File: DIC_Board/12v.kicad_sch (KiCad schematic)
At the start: 31 parts, among them Q100 CSD18542KTTT, Q101 CSD18542KTTT, U10 TPS552882RPMR

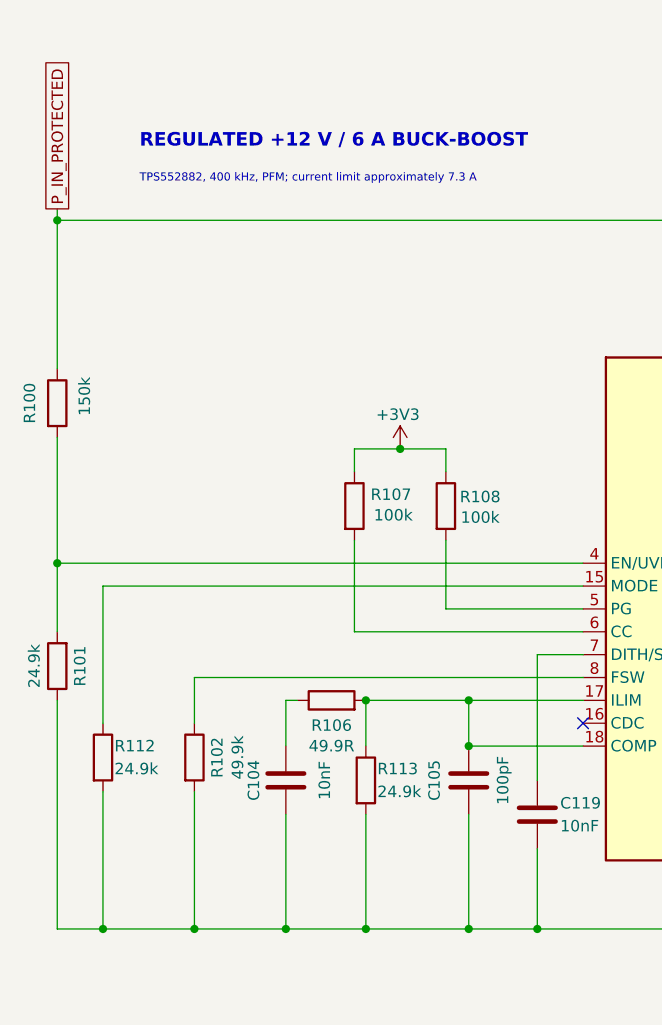
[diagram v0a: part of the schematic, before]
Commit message: Synchronize schematic hierarchy and MCU pin map
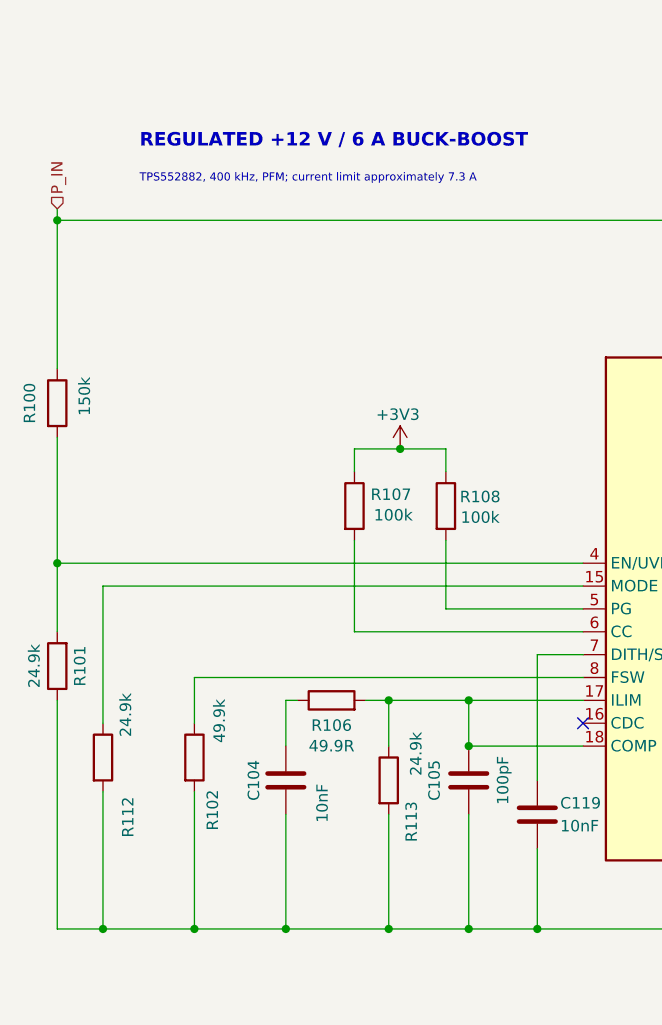
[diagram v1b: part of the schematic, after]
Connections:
- net P_IN_PROTECTED renamed P_IN
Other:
- moved on the sheet: R113
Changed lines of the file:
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@@
 	)
 	(junction
-		(at 73.66 115.57)
-		(diameter 0)
-		(color 0 0 0 0)
-	)
-	(junction
 		(at 156.21 80.01)
 		(diameter 0)
@@
 	)
 	(junction
+		(at 76.2 140.97)
+		(diameter 0)
+		(color 0 0 0 0)
+	)
+	(junction
+		(at 76.2 115.57)
+		(diameter 0)
+		(color 0 0 0 0)
+	)
+	(junction
 		(at 85.09 115.57)
 		(diameter 0)
@@
 	)
 	(junction
-		(at 73.66 140.97)
-		(diameter 0)
-		(color 0 0 0 0)
-	)
-	(junction
 		(at 177.8 73.66)
 		(diameter 0)
@@
 	(wire
 		(pts
-			(xy 73.66 128.27) (xy 73.66 140.97)
+			(xy 76.2 128.27) (xy 76.2 140.97)
 		)
 		(stroke
@@
 	(wire
 		(pts
+			(xy 76.2 115.57) (xy 73.66 115.57)
+		)
+		(stroke
+			(width 0)
+			(type default)
+		)
+	)
+	(wire
+		(pts
 			(xy 177.8 73.66) (xy 177.8 74.93)
 		)
@@
 	(wire
 		(pts
-			(xy 85.09 140.97) (xy 73.66 140.97)
+			(xy 85.09 140.97) (xy 76.2 140.97)
 		)
 		(stroke
@@
 	(wire
 		(pts
+			(xy 76.2 115.57) (xy 85.09 115.57)
+		)
+		(stroke
+			(width 0)
+			(type default)
+		)
+	)
+	(wire
+		(pts
 			(xy 237.49 111.76) (xy 237.49 121.92)
 		)
@@
 	(wire
 		(pts
-			(xy 73.66 115.57) (xy 73.66 120.65)
+			(xy 76.2 115.57) (xy 76.2 120.65)
 		)
 		(stroke
@@
 	(wire
 		(pts
-			(xy 73.66 140.97) (xy 64.77 140.97)
+			(xy 64.77 140.97) (xy 76.2 140.97)
 		)
 		(stroke
@@
 	(wire
 		(pts
-			(xy 73.66 115.57) (xy 85.09 115.57)
-		)
-		(stroke
-			(width 0)
-			(type default)
-		)
-	)
-	(wire
-		(pts
 			(xy 97.79 120.65) (xy 85.09 120.65)
 		)
@@
 		)
 	)
-	(global_label "P_IN_PROTECTED"
-		(shape passive)
+	(hierarchical_label "P_IN"
+		(shape input)
 		(at 39.37 60.96 90)
 		(effects
@@
 			(justify left)
 		)
-		(property "Intersheetrefs" "${INTERSHEET_REFS}"
-			(at 39.37 60.96 90)
-			(hide yes)
-			(show_name no)
-			(do_not_autoplace no)
-			(effects
-				(font
-					(size 1.27 1.27)
-				)
-			)
-		)
 	)
 	(symbol
@@
 		(dnp no)
 		(property "Reference" "R102"
-			(at 57.15 121.92 90)
+			(at 56.642 127.762 90)
 			(show_name no)
 			(do_not_autoplace no)
@@
 		)
 		(property "Value" "49.9k"
-			(at 59.436 121.92 90)
+			(at 57.404 117.856 90)
 			(show_name no)
 			(do_not_autoplace no)
@@
 	(symbol
 		(lib_id "Device:R")
-		(at 73.66 124.46 0)
+		(at 76.2 124.46 0)
 		(unit 1)
 		(body_style 1)
@@
 		(dnp no)
 		(property "Reference" "R113"
-			(at 74.93 123.19 0)
+			(at 78.74 131.318 90)
 			(show_name no)
 			(do_not_autoplace no)
@@
 		)
 		(property "Value" "24.9k"
-			(at 74.93 125.73 0)
+			(at 79.248 123.952 90)
 			(show_name no)
 			(do_not_autoplace no)
@@
 		)
 		(property "Footprint" "Resistor_SMD:R_0402_1005Metric"
-			(at 71.882 124.46 90)
+			(at 74.422 124.46 90)
 			(hide yes)
 			(show_name no)
@@
 		)
 		(property "Datasheet" ""
-			(at 73.66 124.46 0)
+			(at 76.2 124.46 0)
 			(hide yes)
 			(show_name no)
@@
 		)
 		(property "Description" "Inductor current-limit programming resistor"
-			(at 73.66 124.46 0)
+			(at 76.2 124.46 0)
 			(hide yes)
 			(show_name no)
@@
 		(dnp no)
 		(property "Reference" "R112"
-			(at 45.72 120.65 0)
+			(at 47.244 130.81 90)
 			(show_name no)
 			(do_not_autoplace no)
@@
 		)
 		(property "Value" "24.9k"
-			(at 45.72 123.19 0)
+			(at 46.99 119.634 90)
 			(show_name no)
 			(do_not_autoplace no)
@@
 		)
 		(property "Value" "10nF"
-			(at 69.088 124.46 90)
+			(at 68.834 127 90)
 			(show_name no)
 			(do_not_autoplace no)

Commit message: Synchronize power, communications, and MCU configuration
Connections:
- net at R106.2, R113.1, U10.17 (ILIM): no longer C105.1, U10.18 (COMP)
- new net: C105.1, U10.18 (COMP)
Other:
- note added: "TPS552882, 400 kHz, PFM current limit approximately 7.3 A"
- note removed: "TPS552882, 400 kHz, PFM; current limit approximately 7.3 A"
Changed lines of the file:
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@@
 	(generator_version "10.0")
 	(paper "A4")
-	(text "TPS552882, 400 kHz, PFM; current limit approximately 7.3 A"
+	(text "TPS552882, 400 kHz, PFM current limit approximately 7.3 A"
 		(exclude_from_sim no)
 		(at 48.514 58.166 0)
@@
 	)
 	(junction
-		(at 85.09 115.57)
-		(diameter 0)
-		(color 0 0 0 0)
-	)
-	(junction
 		(at 181.61 111.76)
 		(diameter 0)
@@
 	(junction
 		(at 256.54 111.76)
-		(diameter 0)
-		(color 0 0 0 0)
-	)
-	(junction
-		(at 85.09 120.65)
 		(diameter 0)
 		(color 0 0 0 0)
@@
 	(wire
 		(pts
-			(xy 85.09 120.65) (xy 85.09 115.57)
-		)
-		(stroke
-			(width 0)
-			(type default)
-		)
-	)
-	(wire
-		(pts
 			(xy 54.61 125.73) (xy 54.61 140.97)
 		)
@@
 	(wire
 		(pts
-			(xy 85.09 115.57) (xy 97.79 115.57)
+			(xy 76.2 115.57) (xy 97.79 115.57)
 		)
 		(stroke
@@
 		)
 		(stroke
-			(width 0)
-			(type default)
-		)
-	)
-	(wire
-		(pts
-			(xy 76.2 115.57) (xy 85.09 115.57)
-		)
-		(stroke

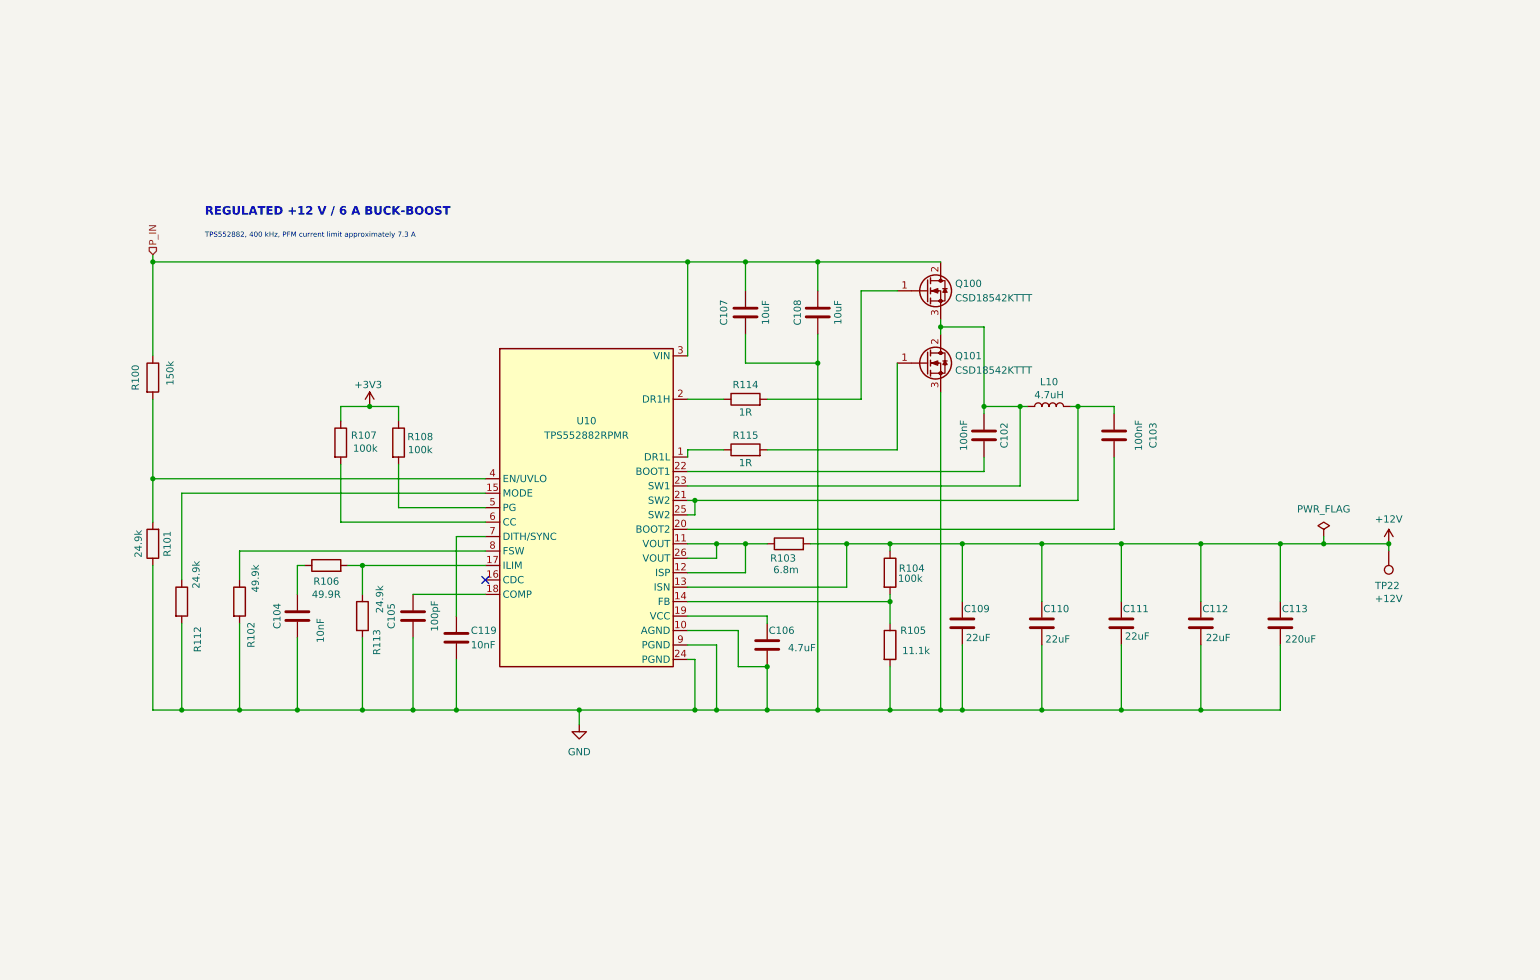
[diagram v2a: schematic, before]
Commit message: Pump fixes + doc extraction
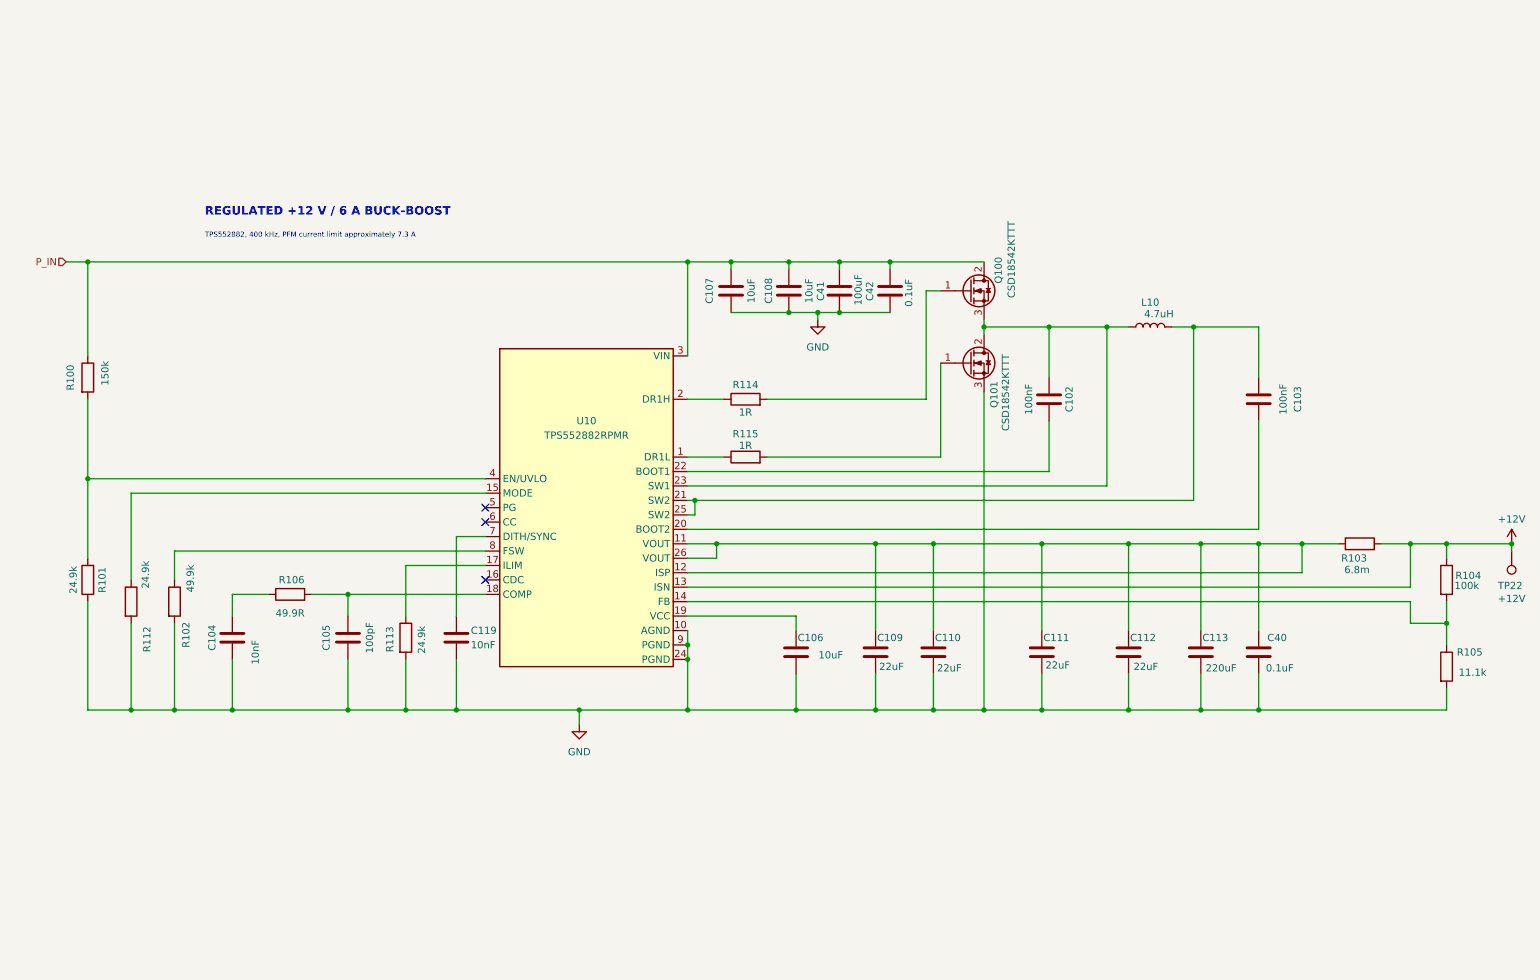
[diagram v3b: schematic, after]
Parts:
- removed R107, R108: 100k, Resistor_SMD:R_0402_1005Metric, symbol Device:R
- added C40, C42: 0.1uF, symbol Device:C
- added C41: 100uF, symbol Device:C
- C106: value 4.7uF -> 10uF; footprint Capacitor_SMD:C_0603_1608Metric -> Capacitor_SMD:C_1206_3216Metric; MPN GRT188R61C475KE13D -> GRM31CR71E106KA12L
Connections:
- net +12V: no longer C109.1, C110.1, C111.1, C112.1, C113.1
- net GND: now also C40.2, C41.2, C42.2
- net P_IN: now also C41.1, C42.1
- net at R113.1, U10.17 (ILIM): no longer R106.2
- net at C105.1, U10.18 (COMP): now also R106.2
- net at R103.1, U10.11 (VOUT), U10.12 (ISP)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: now also C109.1, C110.1, C111.1, C112.1, C113.1, C40.1
- no-connect marks 1 -> 3
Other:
- moved on the sheet: C102, C103, C104, C105, C106, C107, C108, C109, C110, C111, C112, C113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

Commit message: Updated board for layout! All footprints added
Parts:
- C104: value 10nF -> 100nF; footprint Capacitor_SMD:C_0402_1005Metric -> Capacitor_SMD:C_0603_1608Metric; BOM Source (none) -> https://product.tdk.com/en/search/capacitor/ceramic/mlcc/in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; Dielectric (none) -> X7R; MPN CGA2B3X7R1H103K050BB -> C1608X7R1H104K080AA; Tolerance (none) -> 10%; Voltage Rating (none) -> 50V
- C105: value 100pF -> 1nF; footprint Capacitor_SMD:C_0402_1005Metric -> Capacitor_SMD:C_0603_1608Metric; BOM Source (none) -> https://product.tdk.com/en/search/capacitor/ceramic/mlcc/in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; Dielectric (none) -> C0G; MPN CGA2B2C0G1H101J050BA -> C1608C0G1H102J080AA; Tolerance (none) -> 5%; Voltage Rating (none) -> 50V
- C109, C110, C111, C112: BOM Source (none) -> https://www.murata.com/en-us/products/productdetail.aspx?pa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; Dielectric (none) -> X7R; MPN GRM32ER71E226M -> GRM32ER71E226ME15L; Tolerance (none) -> 20%; Voltage Rating (none) -> 25V
- C113: symbol Device:C -> Device:C_Polarized
- C119: BOM Source (none) -> https://product.tdk.com/en/search/capacitor/ceramic/mlcc/in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; Dielectric (none) -> X7R; MPN (none) -> CGA2B3X7R1H103K050BB; Manufacturer (none) -> TDK; Tolerance (none) -> 10%; Voltage Rating (none) -> 50V
- C40, C42: footprint (none) -> Capacitor_SMD:C_0603_1608Metric; BOM Source (none) -> https://product.tdk.com/en/search/capacitor/ceramic/mlcc/in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; Dielectric (none) -> X7R; MPN (none) -> C1608X7R1H104K080AA; Manufacturer (none) -> TDK; Tolerance (none) -> 10%; Voltage Rating (none) -> 50V
- C41: footprint (none) -> Capacitor_SMD:CP_Elec_8x10.5; symbol Device:C -> Device:C_Polarized; BOM Source (none) -> https://industrial.panasonic.com/ww/products/pt/hybrid-alum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; MPN (none) -> EEHZA1V101P; Manufacturer (none) -> Panasonic; Voltage Rating (none) -> 35V
- R103: BOM Source (none) -> https://www.vishay.com/docs/30100/wsl.pdf; MPN CSS2H-2512R-L0068F -> WSL25126L800FEA; Manufacturer Bourns -> Vishay; Power Rating (none) -> 1W; Tolerance (none) -> 1%
- R106: value 49.9R -> 10k; BOM Source (none) -> https://www.vishay.com/docs/20035/dcrcwe3.pdf; Design Basis (none) -> TPS552882 SLVSFC5 equations 19-26; power-loop-design.py ave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; MPN CRCW040249R9FKED -> CRCW040210K0FKED; Tolerance (none) -> 1%
- R112, R113: BOM Source (none) -> https://www.vishay.com/docs/20035/dcrcwe3.pdf; MPN (none) -> CRCW040224K9FKED; Manufacturer (none) -> Vishay; Power Rating (none) -> 0.1W; Tolerance (none) -> 1%
- R114, R115: BOM Source (none) -> https://www.vishay.com/docs/20035/dcrcwe3.pdf; MPN (none) -> CRCW06031R00FKEA; Manufacturer (none) -> Vishay; Power Rating (none) -> 0.125W; Tolerance (none) -> 1%
- TP22: now left out of the parts list
- U10: footprint (none) -> DIC_Board:Texas_RPM0026A_TPS552882

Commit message: Let gpt6 astra have a go at routing. bad results.
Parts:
- TP22: footprint TestPoint:TestPoint_Plated_Hole_D2.0mm -> TestPoint:TestPoint_Pad_D1.0mm
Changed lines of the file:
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@@
 			)
 		)
-		(property "Footprint" "TestPoint:TestPoint_Plated_Hole_D2.0mm"
+		(property "Footprint" "TestPoint:TestPoint_Pad_D1.0mm"
 			(at 278.13 113.03 0)
 			(hide yes)
